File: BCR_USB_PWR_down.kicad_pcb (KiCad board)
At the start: 2 copper layers, 13.3 x 14.1 mm, 2 parts, among them CN1 DB9_Female, CN2 UE27AC54100

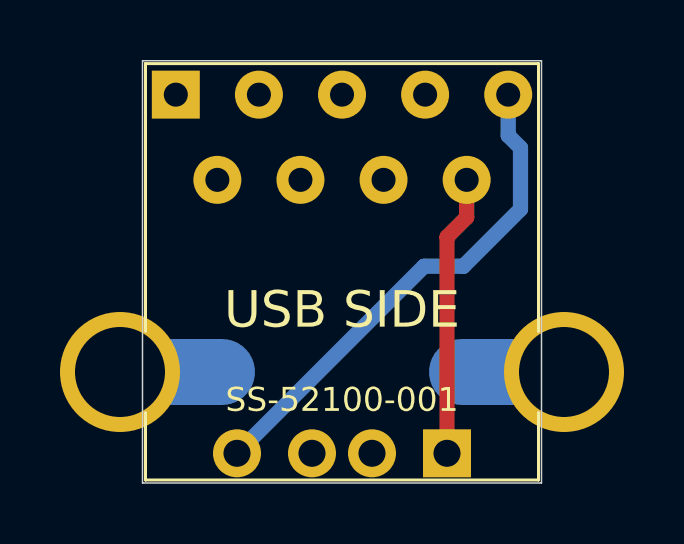
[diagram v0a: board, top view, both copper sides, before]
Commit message: change metal db9 to plastic
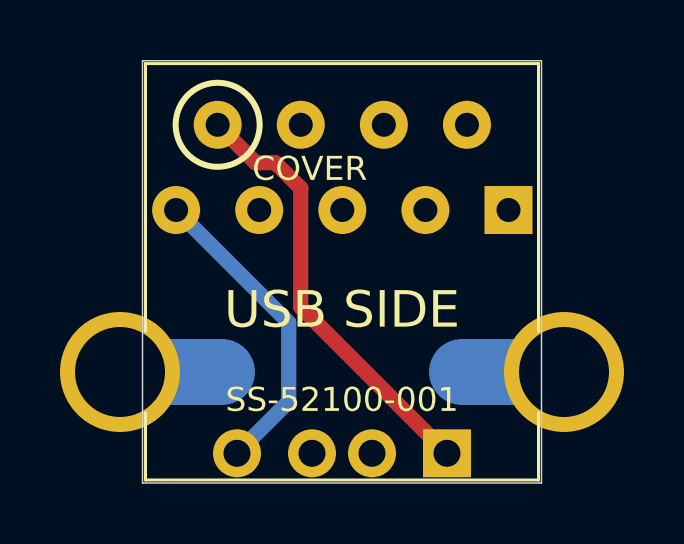
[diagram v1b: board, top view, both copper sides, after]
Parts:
- moved CN1 11.7 mm to (132.6, 98.2), turned to 0 degrees
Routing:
- net /GND: track 16.8 -> 10.4 mm
- net /+5V: track 9.39 -> 14.5 mm
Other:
- board text added: "COVER"
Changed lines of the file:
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@@
   (general
     (thickness 1.6)
-    (drawings 14)
-    (tracks 9)
+    (drawings 16)
+    (tracks 8)
     (zones 0)
     (modules 2)
@@
   )
   (module 0_LOCAL:TE-5207826_cut (layer B.Cu)
-    (at 121.46026 94.33814 180)
+    (at 132.55 98.183)
     (descr "9-pin D-Sub connector, straight/vertical, THT-mount, female, pitch 2.77x2.84mm, distance of mounting holes 25mm, see https://disti-assets.s3.amazonaws.com/tonar/files/datasheets/16730.pdf")
     (tags "9-pin D-Sub connector straight vertical THT female pitch 2.77x2.84mm mounting holes distance 25mm")
@@
     (fp_arc (start 0.703194 0.93) (end 0.703194 2.53) (angle -100) (layer B.Fab) (width 0.1))
     (fp_arc (start -11.783194 0.93) (end -11.783194 2.53) (angle 100) (layer B.Fab) (width 0.1))
-    (pad 9 thru_hole circle (at -9.695 -2.84 180) (size 1.6 1.6) (drill 0.8) (layers *.Cu *.Mask)
+    (pad 9 thru_hole circle (at -9.695 -2.84) (size 1.6 1.6) (drill 0.8) (layers *.Cu *.Mask)
       (net 1 /+5V))
-    (pad 8 thru_hole circle (at -6.925 -2.84 180) (size 1.6 1.6) (drill 0.8) (layers *.Cu *.Mask))
-    (pad 7 thru_hole circle (at -4.155 -2.84 180) (size 1.6 1.6) (drill 0.8) (layers *.Cu *.Mask))
-    (pad 6 thru_hole circle (at -1.385 -2.84 180) (size 1.6 1.6) (drill 0.8) (layers *.Cu *.Mask))
-    (pad 5 thru_hole circle (at -11.08 0 180) (size 1.6 1.6) (drill 0.8) (layers *.Cu *.Mask)
+    (pad 8 thru_hole circle (at -6.925 -2.84) (size 1.6 1.6) (drill 0.8) (layers *.Cu *.Mask))
+    (pad 7 thru_hole circle (at -4.155 -2.84) (size 1.6 1.6) (drill 0.8) (layers *.Cu *.Mask))
+    (pad 6 thru_hole circle (at -1.385 -2.84) (size 1.6 1.6) (drill 0.8) (layers *.Cu *.Mask))
+    (pad 5 thru_hole circle (at -11.08 0) (size 1.6 1.6) (drill 0.8) (layers *.Cu *.Mask)
       (net 2 /GND))
-    (pad 4 thru_hole circle (at -8.31 0 180) (size 1.6 1.6) (drill 0.8) (layers *.Cu *.Mask))
-    (pad 3 thru_hole circle (at -5.54 0 180) (size 1.6 1.6) (drill 0.8) (layers *.Cu *.Mask))
-    (pad 2 thru_hole circle (at -2.77 0 180) (size 1.6 1.6) (drill 0.8) (layers *.Cu *.Mask))
-    (pad 1 thru_hole rect (at 0 0 180) (size 1.6 1.6) (drill 0.8) (layers *.Cu *.Mask))
+    (pad 4 thru_hole circle (at -8.31 0) (size 1.6 1.6) (drill 0.8) (layers *.Cu *.Mask))
+    (pad 3 thru_hole circle (at -5.54 0) (size 1.6 1.6) (drill 0.8) (layers *.Cu *.Mask))
+    (pad 2 thru_hole circle (at -2.77 0) (size 1.6 1.6) (drill 0.8) (layers *.Cu *.Mask))
+    (pad 1 thru_hole rect (at 0 0) (size 1.6 1.6) (drill 0.8) (layers *.Cu *.Mask))
     (model ${KIPRJMOD}/3dmodels/TE-5207826_cut.step
       (offset (xyz -5.528 -1.42 11.5))
@@
     )
   )
-  (gr_text "TE 5207826" (at 127 95.783) (layer B.SilkS)
+  (gr_text COVER (at 125.925 96.808) (layer F.SilkS)
+    (effects (font (size 0.8 0.8) (thickness 0.1)))
+  )
+  (gr_circle (center 122.855 95.343) (end 124.255 95.343) (layer F.SilkS) (width 0.2))
+  (gr_text "TE 5207826" (at 127 96.808) (layer B.SilkS)
     (effects (font (size 0.8 0.8) (thickness 0.1)) (justify mirror))
   )
@@
     (effects (font (size 0.5 0.45) (thickness 0.1)) (justify mirror))
   )
-  (gr_text "BCR to USB 5v" (at 127 101.508) (layer B.SilkS)
+  (gr_text "BCR to USB 5v" (at 127 101.708) (layer B.SilkS)
     (effects (font (size 1.2 1) (thickness 0.2)) (justify mirror))
   )
@@
   (gr_line (start 114.3 87.376) (end 139.7 104.14) (layer Dwgs.User) (width 0.0254))
   (gr_line (start 114.3 104.14) (end 139.7 87.376) (layer Dwgs.User) (width 0.0254))
-  (gr_text "DE9F SIDE" (at 127 98.533) (layer B.SilkS)
+  (gr_text "DE9F SIDE" (at 127 94.108) (layer B.SilkS)
     (effects (font (size 0.8 0.8) (thickness 0.12)) (justify mirror))
   )
@@
     (effects (font (size 1.2192 1.2192) (thickness 0.2032)))
   )
-  (segment (start 130.5 99.083) (end 130.5 106.293) (width 0.508) (layer F.Cu) (net 1))
-  (segment (start 131.15526 97.17814) (end 131.15526 98.42774) (width 0.508) (layer F.Cu) (net 1))
-  (segment (start 131.15526 98.42774) (end 130.5 99.083) (width 0.508) (layer F.Cu) (net 1))
-  (segment (start 132.54026 95.69826) (end 132.54026 94.33814) (width 0.508) (layer B.Cu) (net 2))
-  (segment (start 129.735 100.058) (end 131.05 100.058) (width 0.508) (layer B.Cu) (net 2))
-  (segment (start 132.95 98.158) (end 132.95 96.108) (width 0.508) (layer B.Cu) (net 2))
-  (segment (start 123.5 106.293) (end 129.735 100.058) (width 0.508) (layer B.Cu) (net 2))
-  (segment (start 131.05 100.058) (end 132.95 98.158) (width 0.508) (layer B.Cu) (net 2))
-  (segment (start 132.95 96.108) (end 132.54026 95.69826) (width 0.508) (layer B.Cu) (net 2))
+  (segment (start 125.625 101.418) (end 130.5 106.293) (width 0.508) (layer F.Cu) (net 1))
+  (segment (start 125.625 97.458) (end 125.625 101.418) (width 0.508) (layer F.Cu) (net 1))
+  (segment (start 124.775 96.608) (end 125.625 97.458) (width 0.508) (layer F.Cu) (net 1))
+  (segment (start 122.855 95.343) (end 124.12 96.608) (width 0.508) (layer F.Cu) (net 1))
+  (segment (start 124.12 96.608) (end 124.775 96.608) (width 0.508) (layer F.Cu) (net 1))
+  (segment (start 125.225 101.938) (end 121.47 98.183) (width 0.508) (layer B.Cu) (net 2))
+  (segment (start 123.5 106.293) (end 125.225 104.568) (width 0.508) (layer B.Cu) (net 2))
+  (segment (start 125.225 104.568) (end 125.225 101.938) (width 0.508) (layer B.Cu) (net 2))
 )

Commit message: db9 pin 7 is the real GND, not pin 5
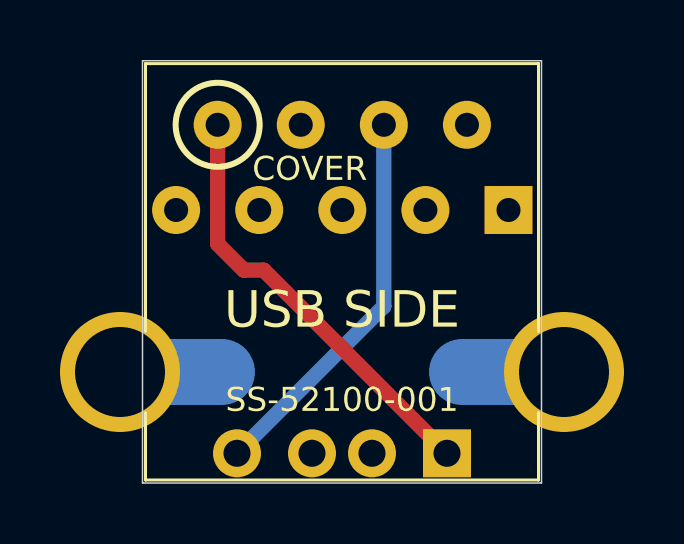
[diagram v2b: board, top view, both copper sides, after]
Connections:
- CN1 pad 5: /GND -> (no net)
- CN1 pad 7: (no net) -> /GND
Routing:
- net /GND: track 10.4 -> 13.0 mm
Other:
- net class Default: clearance 0.2 -> 0.16; trace_width 0.25 -> 0.16; via_dia 0.8 -> 0.42; via_drill 0.4 -> 0.26
- rule trace_clearance: 0.2 -> 0.16
- rule trace_min: 0.2 -> 0.16
- rule via_min_drill: 0.3 -> 0.26
- rule via_min_size: 0.4 -> 0.42
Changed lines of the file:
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@@
     (thickness 1.6)
     (drawings 16)
-    (tracks 8)
+    (tracks 6)
     (zones 0)
     (modules 2)
@@
   )
   (setup
-    (last_trace_width 0.25)
-    (user_trace_width 0.508)
-    (trace_clearance 0.2)
+    (last_trace_width 0.16)
+    (user_trace_width 0.5)
+    (trace_clearance 0.16)
     (zone_clearance 0.508)
     (zone_45_only no)
-    (trace_min 0.2)
-    (via_size 0.8)
-    (via_drill 0.4)
-    (via_min_size 0.4)
-    (via_min_drill 0.3)
-    (user_via 0.508 0.3048)
+    (trace_min 0.16)
+    (via_size 0.42)
+    (via_drill 0.26)
+    (via_min_size 0.42)
+    (via_min_drill 0.26)
     (uvia_size 0.3)
     (uvia_drill 0.1)
@@
     (mod_text_width 0.15)
     (pad_size 1.6 1.6)
-    (pad_drill 0.9)
+    (pad_drill 0.8)
     (pad_to_mask_clearance 0)
     (aux_axis_origin 0 0)
@@
   (net 3 "Net-(CN2-PadSH)")
   (net_class Default "This is the default net class."
-    (clearance 0.2)
-    (trace_width 0.25)
-    (via_dia 0.8)
-    (via_drill 0.4)
+    (clearance 0.16)
+    (trace_width 0.16)
+    (via_dia 0.42)
+    (via_drill 0.26)
     (uvia_dia 0.3)
     (uvia_drill 0.1)
@@
       (effects (font (size 1 1) (thickness 0.15)))
     )
+    (fp_line (start -6.55 -3.6) (end 6.55 -3.6) (layer F.SilkS) (width 0.1))
+    (fp_line (start 6.55 1.35) (end 6.55 10.28) (layer F.SilkS) (width 0.1))
+    (fp_line (start -6.55 1.35) (end -6.55 10.28) (layer F.SilkS) (width 0.1))
+    (fp_line (start -6.55 -3.6) (end -6.55 -1.35) (layer F.SilkS) (width 0.1))
+    (fp_line (start -6.55 -3.6) (end 6.55 -3.6) (layer F.Fab) (width 0.1))
+    (fp_line (start 6.55 -3.6) (end 6.55 10.28) (layer F.Fab) (width 0.1))
+    (fp_line (start -6.55 -3.6) (end -6.55 10.28) (layer F.Fab) (width 0.1))
+    (fp_line (start -6.55 10.28) (end 6.55 10.28) (layer F.Fab) (width 0.1))
+    (fp_line (start 6.55 -3.6) (end 6.55 -1.35) (layer F.SilkS) (width 0.1))
+    (fp_line (start 6.55 10.28) (end -6.55 10.28) (layer F.SilkS) (width 0.1))
+    (fp_line (start -6.75 -3.94) (end 6.75 -3.94) (layer F.CrtYd) (width 0.05))
+    (fp_line (start 6.75 -3.94) (end 6.75 10.375) (layer F.CrtYd) (width 0.05))
+    (fp_line (start -6.75 -3.94) (end -6.75 10.375) (layer F.CrtYd) (width 0.05))
     (fp_line (start -6.75 10.375) (end 6.75 10.375) (layer F.CrtYd) (width 0.05))
-    (fp_line (start -6.75 -3.94) (end -6.75 10.375) (layer F.CrtYd) (width 0.05))
-    (fp_line (start 6.75 -3.94) (end 6.75 10.375) (layer F.CrtYd) (width 0.05))
-    (fp_line (start -6.75 -3.94) (end 6.75 -3.94) (layer F.CrtYd) (width 0.05))
-    (fp_line (start 6.55 10.28) (end -6.55 10.28) (layer F.SilkS) (width 0.1))
-    (fp_line (start 6.55 -3.6) (end 6.55 -1.35) (layer F.SilkS) (width 0.1))
-    (fp_line (start -6.55 10.28) (end 6.55 10.28) (layer F.Fab) (width 0.1))
-    (fp_line (start -6.55 -3.6) (end -6.55 10.28) (layer F.Fab) (width 0.1))
-    (fp_line (start 6.55 -3.6) (end 6.55 10.28) (layer F.Fab) (width 0.1))
-    (fp_line (start -6.55 -3.6) (end 6.55 -3.6) (layer F.Fab) (width 0.1))
-    (fp_line (start -6.55 -3.6) (end -6.55 -1.35) (layer F.SilkS) (width 0.1))
-    (fp_line (start -6.55 1.35) (end -6.55 10.28) (layer F.SilkS) (width 0.1))
-    (fp_line (start 6.55 1.35) (end 6.55 10.28) (layer F.SilkS) (width 0.1))
-    (fp_line (start -6.55 -3.6) (end 6.55 -3.6) (layer F.SilkS) (width 0.1))
     (fp_text user %R (at -0.025 0.975 180) (layer F.Fab)
       (effects (font (size 1 1) (thickness 0.15)))
@@
       (effects (font (size 1 1) (thickness 0.15)) (justify mirror))
     )
+    (fp_line (start -6.54 -1.42) (end -4.54 -1.42) (layer Dwgs.User) (width 0.01))
+    (fp_line (start -5.54 -0.82) (end -5.54 -2.02) (layer Dwgs.User) (width 0.01))
+    (fp_line (start -11.783194 2.53) (end 0.703194 2.53) (layer B.Fab) (width 0.1))
+    (fp_line (start -10.954457 -5.37) (end -0.125543 -5.37) (layer B.Fab) (width 0.1))
+    (fp_line (start 2.278887 0.652163) (end 1.45015 -4.047837) (layer B.Fab) (width 0.1))
+    (fp_line (start -13.358887 0.652163) (end -12.53015 -4.047837) (layer B.Fab) (width 0.1))
+    (fp_line (start -11.771689 2.59) (end 0.691689 2.59) (layer B.SilkS) (width 0.12))
+    (fp_line (start -10.942952 -5.43) (end -0.137048 -5.43) (layer B.SilkS) (width 0.12))
+    (fp_line (start 2.32647 0.641744) (end 1.497733 -4.058256) (layer B.SilkS) (width 0.12))
+    (fp_line (start -13.40647 0.641744) (end -12.577733 -4.058256) (layer B.SilkS) (width 0.12))
+    (fp_line (start -13.95 3.91) (end -13.95 -6.74) (layer B.CrtYd) (width 0.05))
+    (fp_line (start -13.95 -6.74) (end 2.9 -6.74) (layer B.CrtYd) (width 0.05))
+    (fp_line (start 2.9 -6.74) (end 2.9 3.91) (layer B.CrtYd) (width 0.05))
     (fp_line (start 2.9 3.91) (end -13.95 3.91) (layer B.CrtYd) (width 0.05))
-    (fp_line (start 2.9 -6.74) (end 2.9 3.91) (layer B.CrtYd) (width 0.05))
-    (fp_line (start -13.95 -6.74) (end 2.9 -6.74) (layer B.CrtYd) (width 0.05))
-    (fp_line (start -13.95 3.91) (end -13.95 -6.74) (layer B.CrtYd) (width 0.05))
-    (fp_line (start -13.40647 0.641744) (end -12.577733 -4.058256) (layer B.SilkS) (width 0.12))
-    (fp_line (start 2.32647 0.641744) (end 1.497733 -4.058256) (layer B.SilkS) (width 0.12))
-    (fp_line (start -10.942952 -5.43) (end -0.137048 -5.43) (layer B.SilkS) (width 0.12))
-    (fp_line (start -11.771689 2.59) (end 0.691689 2.59) (layer B.SilkS) (width 0.12))
-    (fp_line (start -13.358887 0.652163) (end -12.53015 -4.047837) (layer B.Fab) (width 0.1))
-    (fp_line (start 2.278887 0.652163) (end 1.45015 -4.047837) (layer B.Fab) (width 0.1))
-    (fp_line (start -10.954457 -5.37) (end -0.125543 -5.37) (layer B.Fab) (width 0.1))
-    (fp_line (start -11.783194 2.53) (end 0.703194 2.53) (layer B.Fab) (width 0.1))
-    (fp_line (start -5.54 -0.82) (end -5.54 -2.02) (layer Dwgs.User) (width 0.01))
-    (fp_line (start -6.54 -1.42) (end -4.54 -1.42) (layer Dwgs.User) (width 0.01))
     (fp_text user %R (at -5.54 -1.42 180) (layer B.Fab)
       (effects (font (size 1 1) (thickness 0.15)) (justify mirror))
@@
       (net 1 /+5V))
     (pad 8 thru_hole circle (at -6.925 -2.84) (size 1.6 1.6) (drill 0.8) (layers *.Cu *.Mask))
-    (pad 7 thru_hole circle (at -4.155 -2.84) (size 1.6 1.6) (drill 0.8) (layers *.Cu *.Mask))
+    (pad 7 thru_hole circle (at -4.155 -2.84) (size 1.6 1.6) (drill 0.8) (layers *.Cu *.Mask)
+      (net 2 /GND))
     (pad 6 thru_hole circle (at -1.385 -2.84) (size 1.6 1.6) (drill 0.8) (layers *.Cu *.Mask))
-    (pad 5 thru_hole circle (at -11.08 0) (size 1.6 1.6) (drill 0.8) (layers *.Cu *.Mask)
-      (net 2 /GND))
+    (pad 5 thru_hole circle (at -11.08 0) (size 1.6 1.6) (drill 0.8) (layers *.Cu *.Mask))
     (pad 4 thru_hole circle (at -8.31 0) (size 1.6 1.6) (drill 0.8) (layers *.Cu *.Mask))
     (pad 3 thru_hole circle (at -5.54 0) (size 1.6 1.6) (drill 0.8) (layers *.Cu *.Mask))
@@
     (effects (font (size 1.2192 1.2192) (thickness 0.2032)))
   )
-  (segment (start 125.625 101.418) (end 130.5 106.293) (width 0.508) (layer F.Cu) (net 1))
-  (segment (start 125.625 97.458) (end 125.625 101.418) (width 0.508) (layer F.Cu) (net 1))
-  (segment (start 124.775 96.608) (end 125.625 97.458) (width 0.508) (layer F.Cu) (net 1))
-  (segment (start 122.855 95.343) (end 124.12 96.608) (width 0.508) (layer F.Cu) (net 1))
-  (segment (start 124.12 96.608) (end 124.775 96.608) (width 0.508) (layer F.Cu) (net 1))
-  (segment (start 125.225 101.938) (end 121.47 98.183) (width 0.508) (layer B.Cu) (net 2))
-  (segment (start 123.5 106.293) (end 125.225 104.568) (width 0.508) (layer B.Cu) (net 2))
-  (segment (start 125.225 104.568) (end 125.225 101.938) (width 0.508) (layer B.Cu) (net 2))
+  (segment (start 124.395 100.188) (end 130.5 106.293) (width 0.508) (layer F.Cu) (net 1))
+  (segment (start 123.73 100.188) (end 124.395 100.188) (width 0.508) (layer F.Cu) (net 1))
+  (segment (start 122.855 95.343) (end 122.855 99.313) (width 0.508) (layer F.Cu) (net 1))
+  (segment (start 122.855 99.313) (end 123.73 100.188) (width 0.508) (layer F.Cu) (net 1))
+  (segment (start 128.395 101.398) (end 128.395 95.343) (width 0.508) (layer B.Cu) (net 2))
+  (segment (start 123.5 106.293) (end 128.395 101.398) (width 0.508) (layer B.Cu) (net 2))
 )
